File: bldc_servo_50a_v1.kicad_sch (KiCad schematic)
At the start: 132 parts, among them J1 CAN1, J2 CAN2, J3 FAN, J5 SWD, P1 PVDD, P2 GND, P3 PHASE_A, P4 PHASE_B, P5 PHASE_C, Q1 BSC010N04LS, Q2 BSC010N04LS, Q3 BSC010N04LS, Q4 BSC010N04LS, Q5 BSC010N04LS, Q6 BSC010N04LS, U1 STM32G431CBT6, U2 DRV8305NQPHPRQ1, U3 LMR51430, U4 TLV75533PDBV, U5 SN65HVD230, U6 TPS22919DCKR

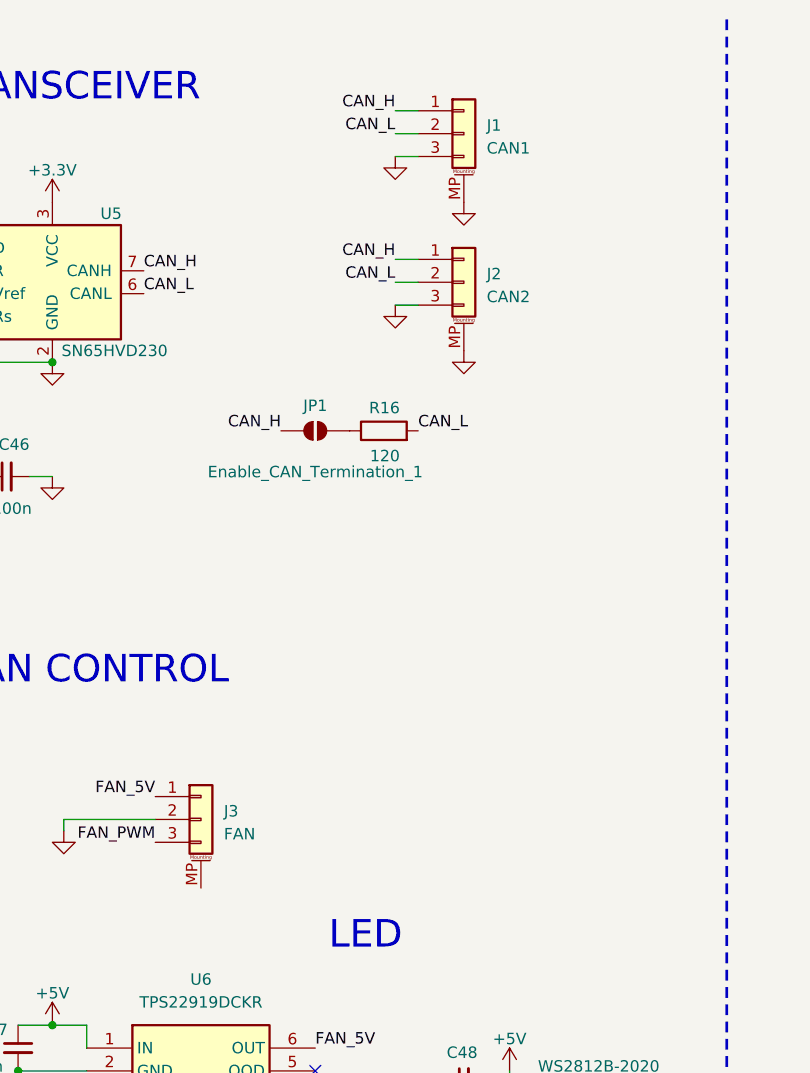
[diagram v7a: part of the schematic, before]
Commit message: Added TVS for CAN
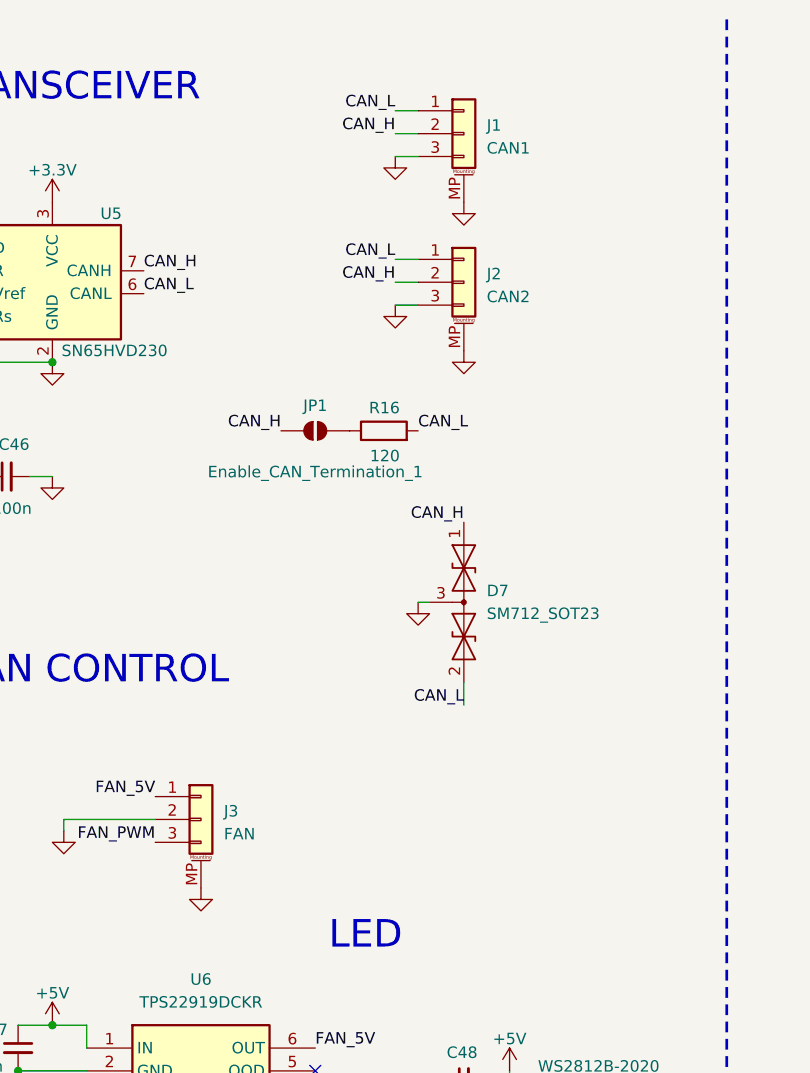
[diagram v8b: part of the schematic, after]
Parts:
- added D7: SM712_SOT23, Package_TO_SOT_SMD:SOT-23, symbol Diode:SM712_SOT23
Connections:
- net CAN_H: now also J1.2 (Pin_2), J2.2 (Pin_2), D7.1 (A1); no longer J1.1 (Pin_1), J2.1 (Pin_1)
- net CAN_L: now also J1.1 (Pin_1), J2.1 (Pin_1), D7.2 (A2); no longer J1.2 (Pin_2), J2.2 (Pin_2)
- net GND: now also J3.MP (MountPin), D7.3 (common)
